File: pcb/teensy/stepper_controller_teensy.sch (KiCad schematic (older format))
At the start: 20 parts, among them P1 TERM_BLK_ANG_4_PIN_0.2_PITCH, P2 PWR_JACK_2.5x5.5, SW1 SPST_SLIDE_AS, SW2 SPST_PUSH_LIGHTS, SW3 KT_SWITCH, T1 TERM_BLK_2_PIN_0.1_PITCH, U1 L6470, U2 MAX6817

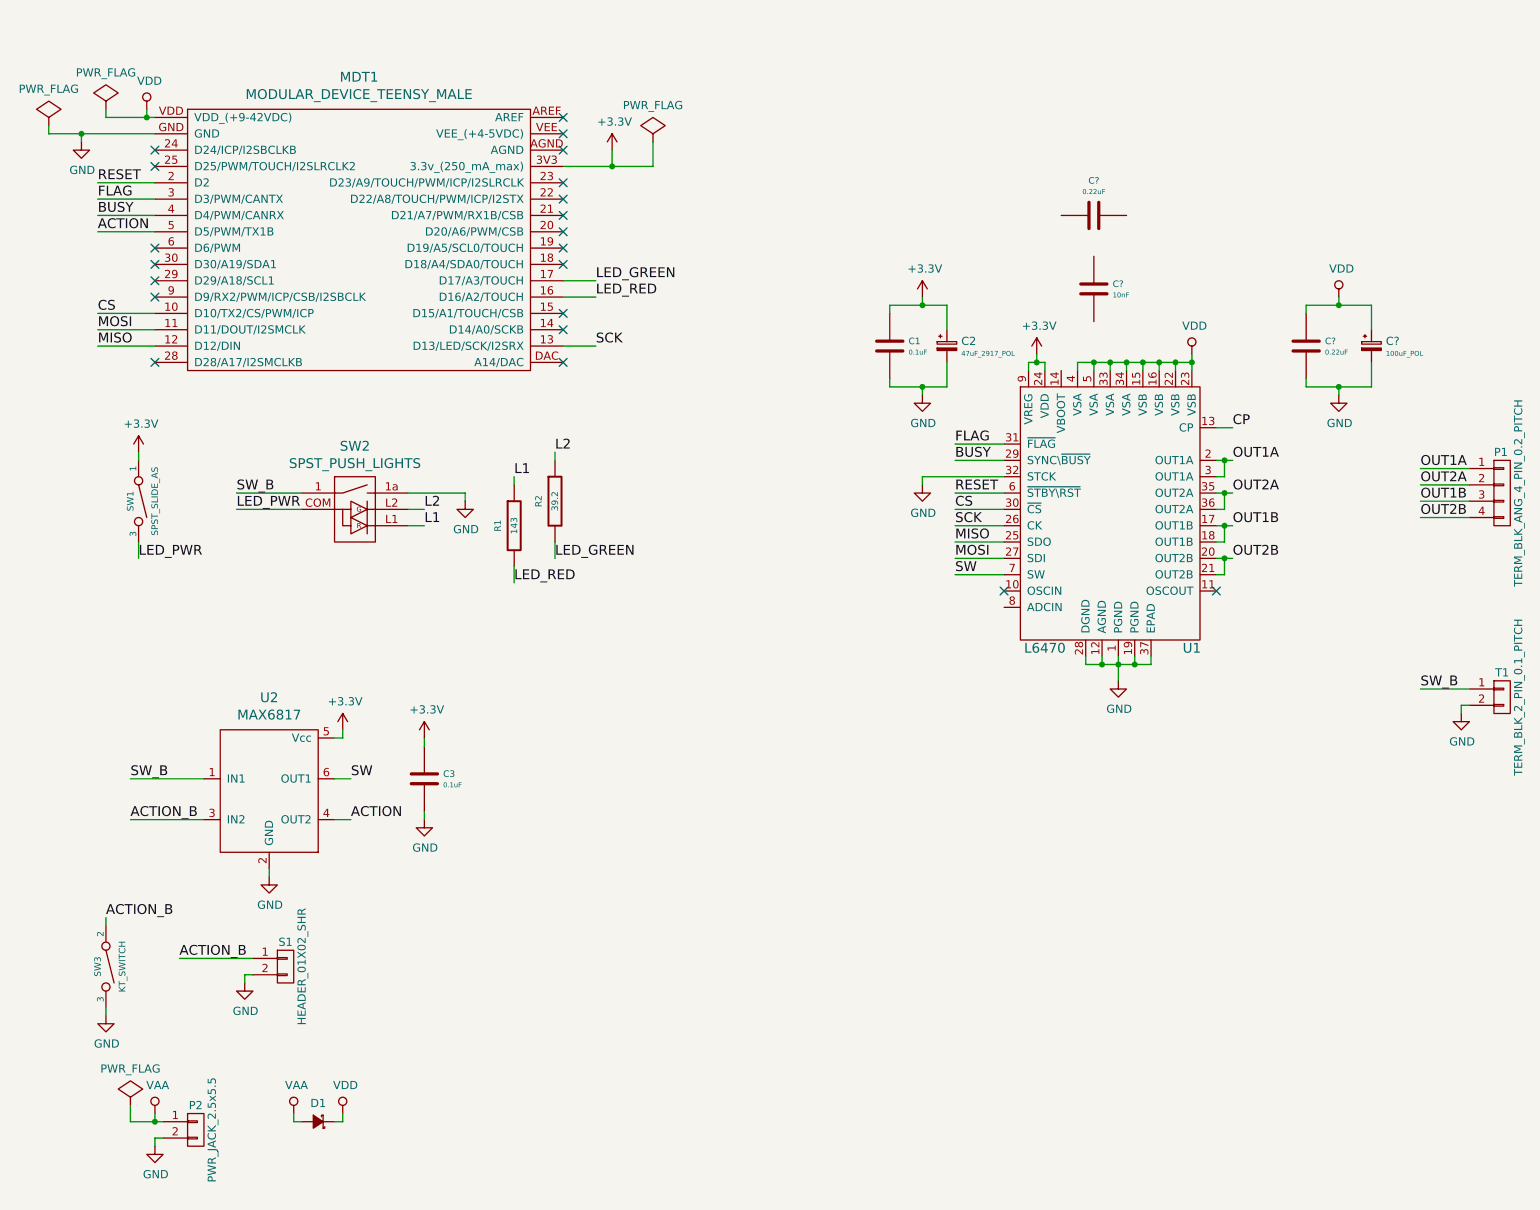
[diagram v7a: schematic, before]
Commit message: Added components.
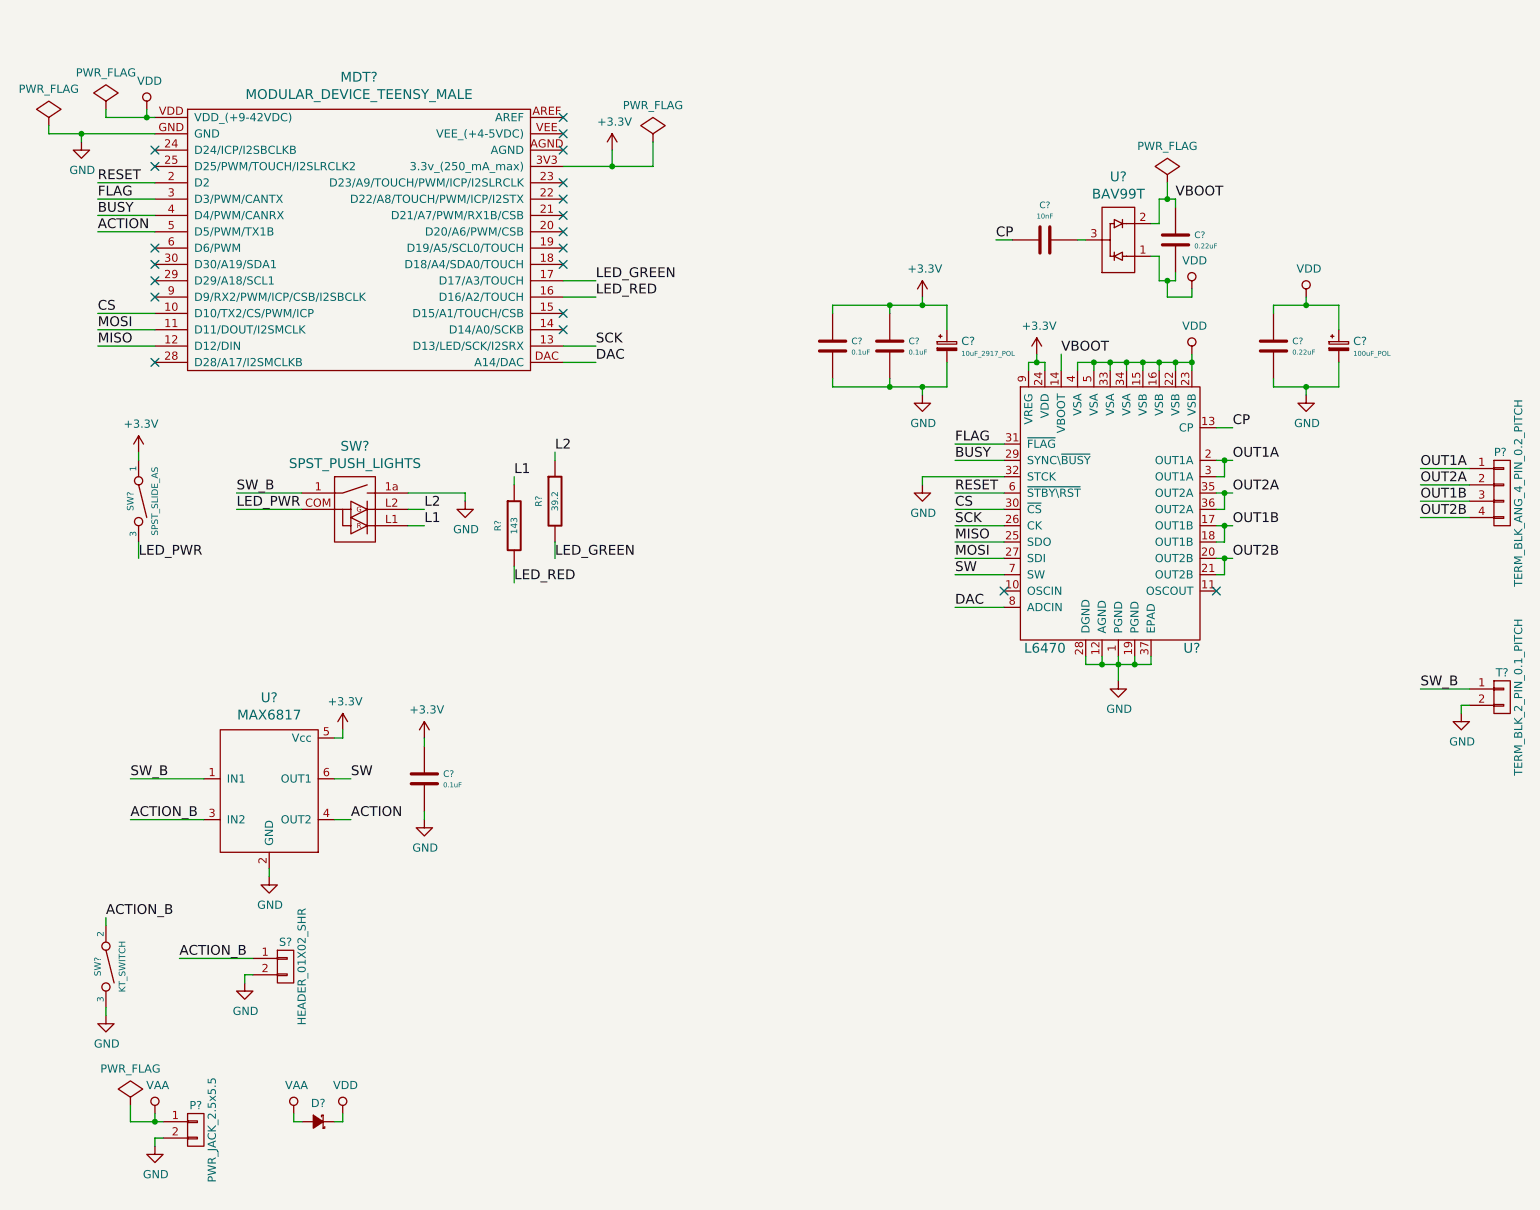
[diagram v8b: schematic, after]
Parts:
- removed C2: 47uF_2917_POL, footprints:SM2917_POL, symbol 47uF_2917_POL
- added C?: 0.1uF, stepper_controller_teensy:SM1210, symbol 0.1uF
- added C?: 10uF_2917_POL, stepper_controller_teensy:SM2917_POL, symbol 10uF_2917_POL
- added U?: BAV99T, stepper_controller_teensy:SOT-523, symbol BAV99T
- C?: renamed from C3; footprint footprints:SM1210 -> stepper_controller_teensy:SM1210
- C?: renamed from C1; footprint footprints:SM1210 -> stepper_controller_teensy:SM1210
- C? (x3): footprint footprints:SM1210 -> stepper_controller_teensy:SM1210
- C?: footprint footprints:C_ELEC_12.5 -> stepper_controller_teensy:C_ELEC_12.5
- D?: renamed from D1; footprint footprints:CFP15 -> stepper_controller_teensy:CFP15
- P?: renamed from P1; footprint footprints:TERM_BLK_ANG_4_PIN_0.2_PITCH -> stepper_controller_teensy:TERM_BLK_ANG_4_PIN_0.2_PITCH
- P?: renamed from P2; footprint footprints:DCJACK_2PIN_HIGHCURRENT -> stepper_controller_teensy:DCJACK_2PIN_HIGHCURRENT
- R?: renamed from R1; footprint footprints:SM1210 -> stepper_controller_teensy:SM1210
- R?: renamed from R2; footprint footprints:SM1210 -> stepper_controller_teensy:SM1210
- S?: renamed from S1; footprint footprints:Header_Shrouded_2_Pin -> stepper_controller_teensy:Header_Shrouded_2_Pin
- SW?: renamed from SW3; footprint footprints:KT_SWITCH -> stepper_controller_teensy:KT_SWITCH
- SW?: renamed from SW2; footprint footprints:KP_SWITCH -> stepper_controller_teensy:KP_SWITCH
- T?: renamed from T1; footprint footprints:TERM_BLK_2_PIN_0.1_PITCH -> stepper_controller_teensy:TERM_BLK_2_PIN_0.1_PITCH
- U?: renamed from U2; footprint footprints:MAX6817 -> stepper_controller_teensy:MAX6817
- U?: renamed from U1; footprint footprints:POWERSO-36 -> stepper_controller_teensy:POWERSO-36
- renumbered MDT1 to MDT?, SW1 to SW?
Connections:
- net +3V3: now also C?.1, C?.1
- net CP: now also C?.1
- net GND: now also C?.2, C?.2
- net VDD: now also C?.1, U?.1
- net DAC: now reaches MDT?.DAC (A14/DAC)
- net DAC: now also U?.8 (ADCIN)
- net VBOOT: now reaches U?.14 (VBOOT)
- net VBOOT: now also C?.2, U?.2
- net at C?.2: now also U?.3
- no-connect marks 21 -> 20
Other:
- moved on the sheet: C?
